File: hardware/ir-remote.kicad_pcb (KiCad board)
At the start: 2 copper layers, 30 x 58 mm, 42 parts, among them J1 USB-C USB2.0, J2 LiPo 400-500mAh, Q1 AO3400A, Q2 AO3400A, SW1 BTN1, SW2 BTN2, SW3 BTN3, SW4 BTN4, SW5 BTN5, SW6 BOOT, SW7 RESET, U1 ESP32-S3-WROOM-1-N8, U2 HT7833, U3 MCP73831-2-OT, U4 USBLC6-2SC6

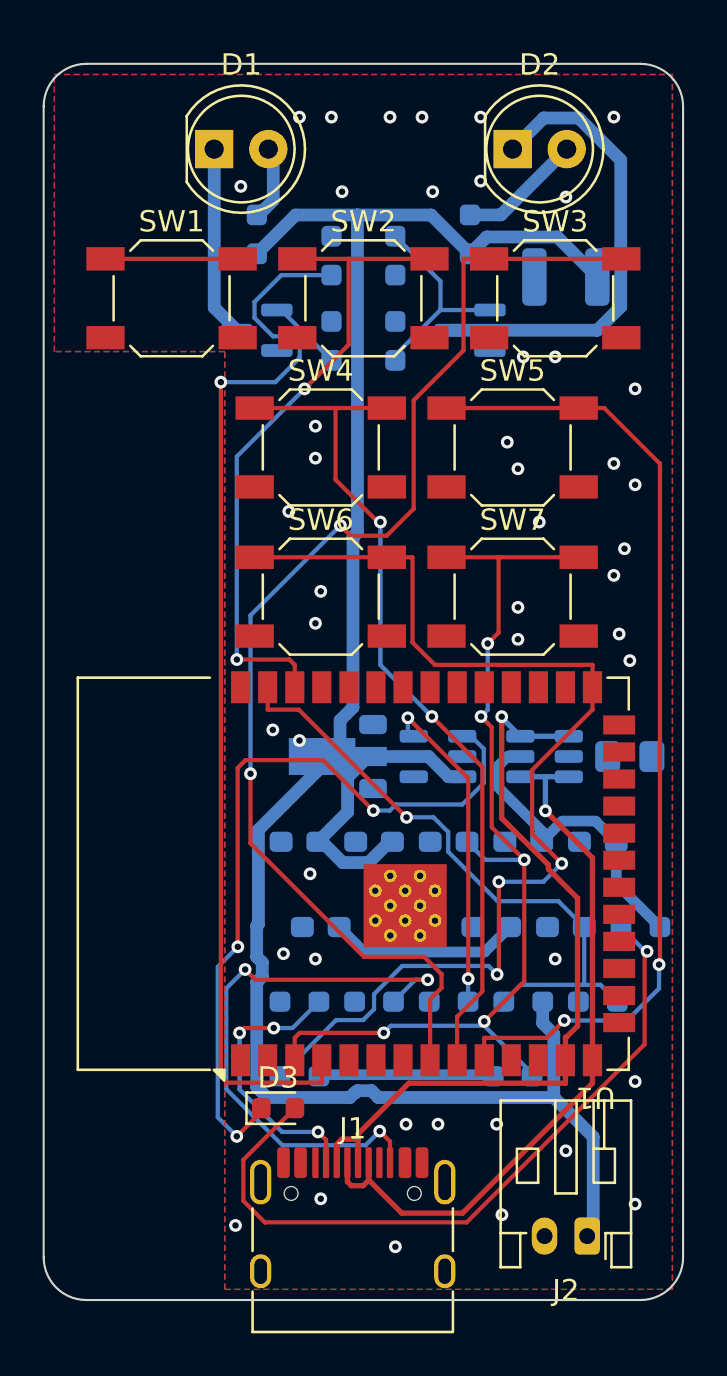
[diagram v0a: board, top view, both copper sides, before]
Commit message: hardware: GND cannot be carried by the pour on this board -- diagnosis + state
DRC still 0 violations at JLCPCB rules, antenna keepout verified clear by direct
copper audit. 295 tracks, 131 vias, both GND pours restored. 26 unconnected
items remain (GND 32 endpoints, +3V3 8, VBUS 6, and three signal nets).

Key finding, which cost several iterations and would otherwise have shipped as a
dead board:

  - Pours on both layers plus 90 stitching vias still left ~32 GND endpoints
    unconnected, and each batch of vias barely moved it (44 -> 42 -> 38 -> 34 ->
    32). The back side is too dense for the pour to weave through: KiCad's fill
    fragments into 14 pieces on F.Cu and 15 on B.Cu, and several GND pads sit
    where no fragment reaches -- so stitching vias cannot help, there is nothing
    adjacent to stitch to.

  - Freerouting exported the pours as planes and therefore assumed GND was
    already connected, emitting a single GND wire across two full passes. The
    board had ZERO routed GND segments while looking entirely plausible.

Lesson recorded in DESIGN-pcb.md: on a dense 2-layer board a pour does not
equal connectivity -- check the routed-GND-segment count, not just DRC's
unconnected number.

Pass 3 (pours stripped, GND as an ordinary 0.4mm routable net) is the correct
fix but did not converge in ~35 min and was killed; pours were restored so the
board is not left degraded. Root cause is back-side density, which is a design
decision, not a router-time problem.

No gerbers, no BOM, no fab. Nothing here is proven.

Co-Authored-By: Claude Opus 4.8 (1M context) <noreply@anthropic.com>
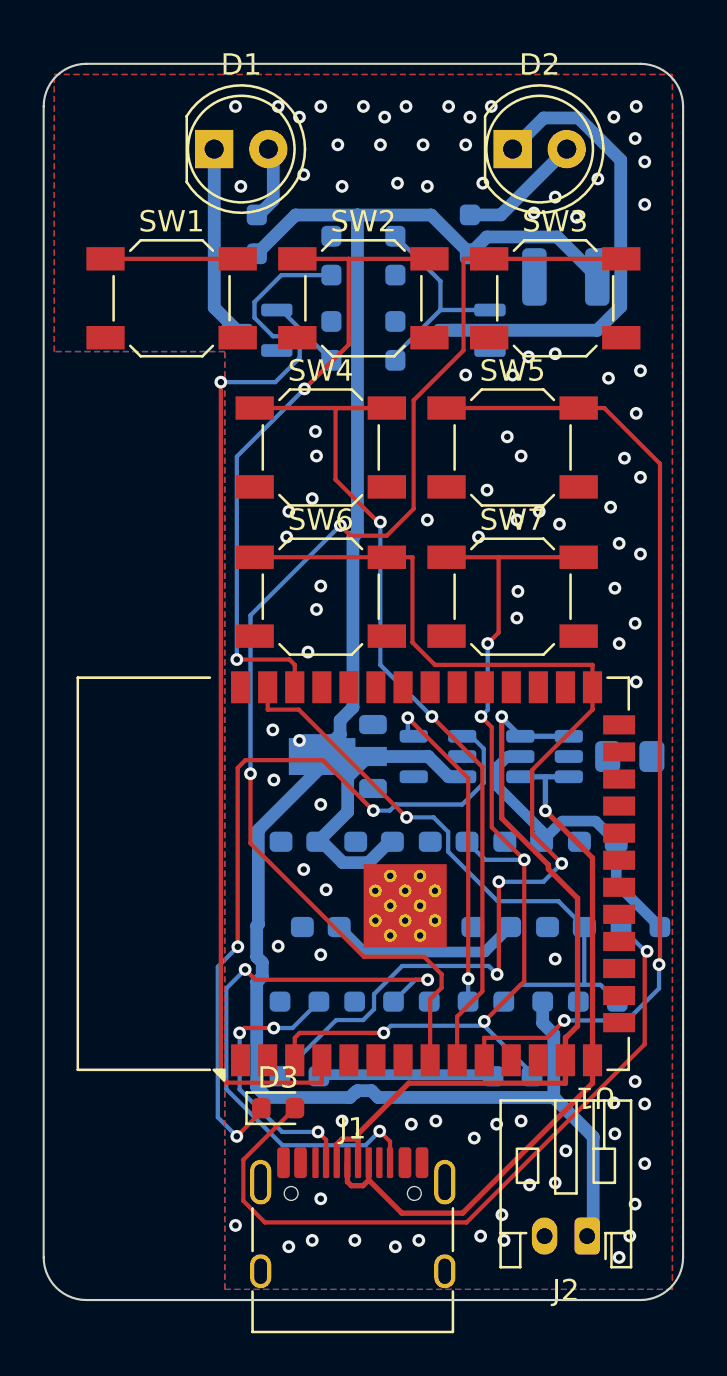
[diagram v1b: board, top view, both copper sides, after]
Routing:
- net BTN4: track 40.2 -> 42.6 mm
- net VBAT: track 103.8 -> 105.8 mm
- net GND: vias 8 -> 98
- net (no net): vias 37 -> 0
